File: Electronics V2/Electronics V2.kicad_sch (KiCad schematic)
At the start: 23 parts, among them J1 MOT_L, J2 MOT_R, J3 SD_Card, J4 USB_C_Receptacle_USB2.0_16P, SW1 RST, SW3 RST, SW4 BOOT, U3 ESP32-S3-WROOM-1, U4 DAC081C081CIMK, U5 IMU_L, U6 IMU_R

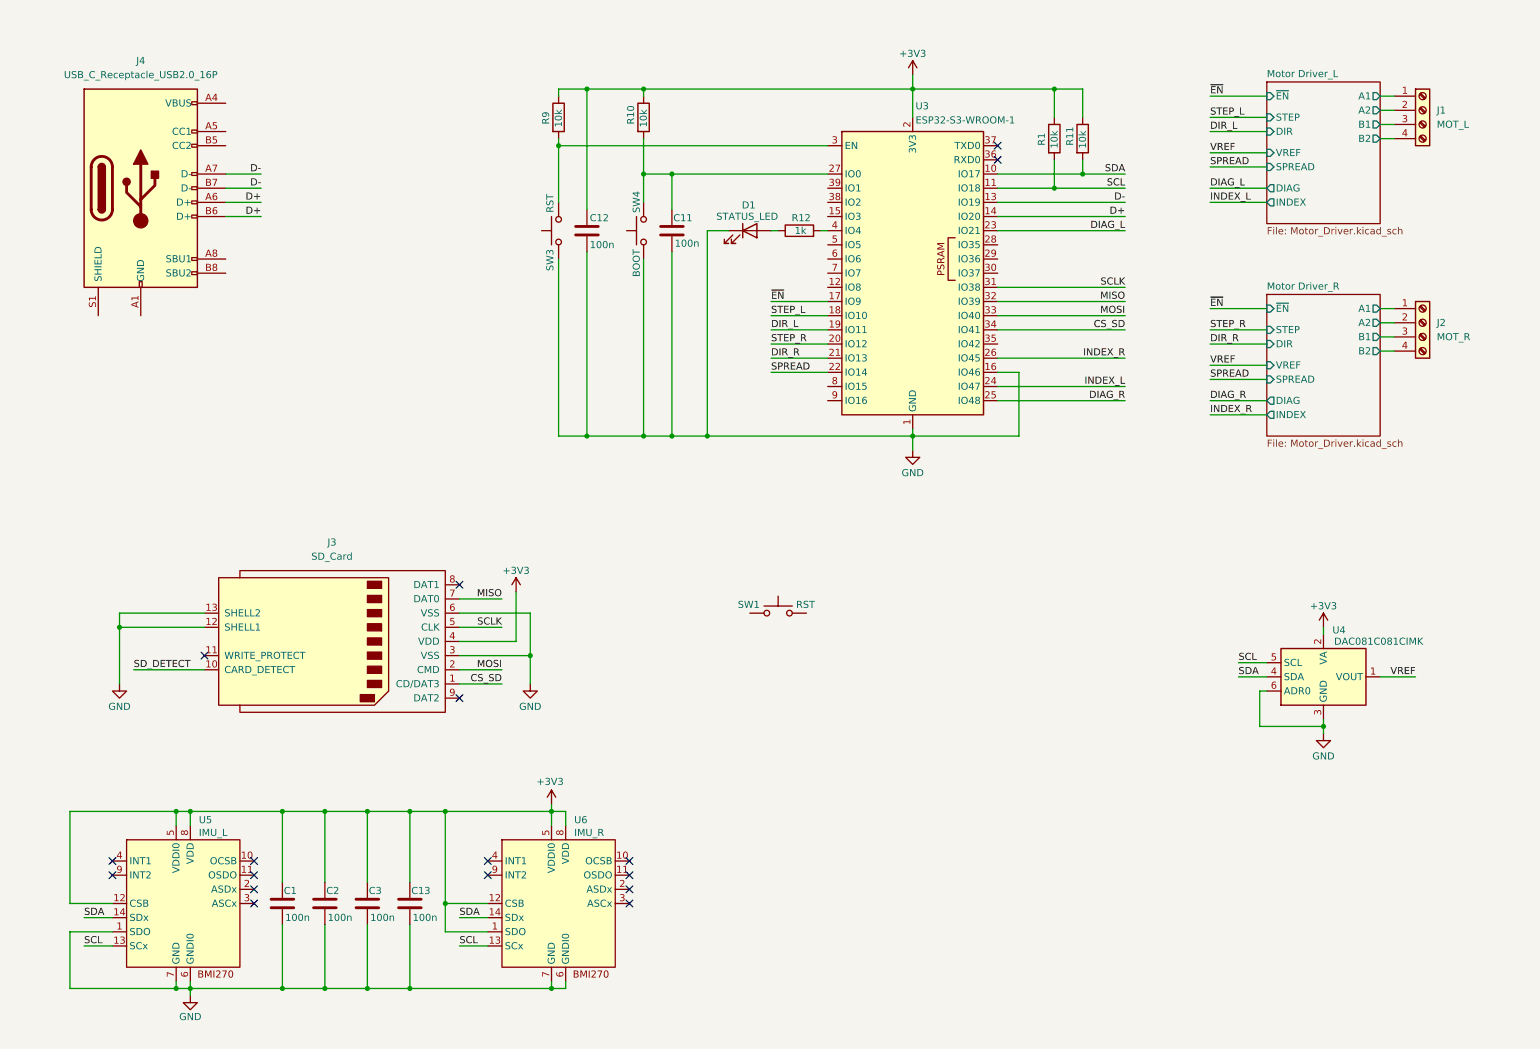
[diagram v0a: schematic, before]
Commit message: rotary encoder, buttons, needs esd, reverse voltage, usb, reg
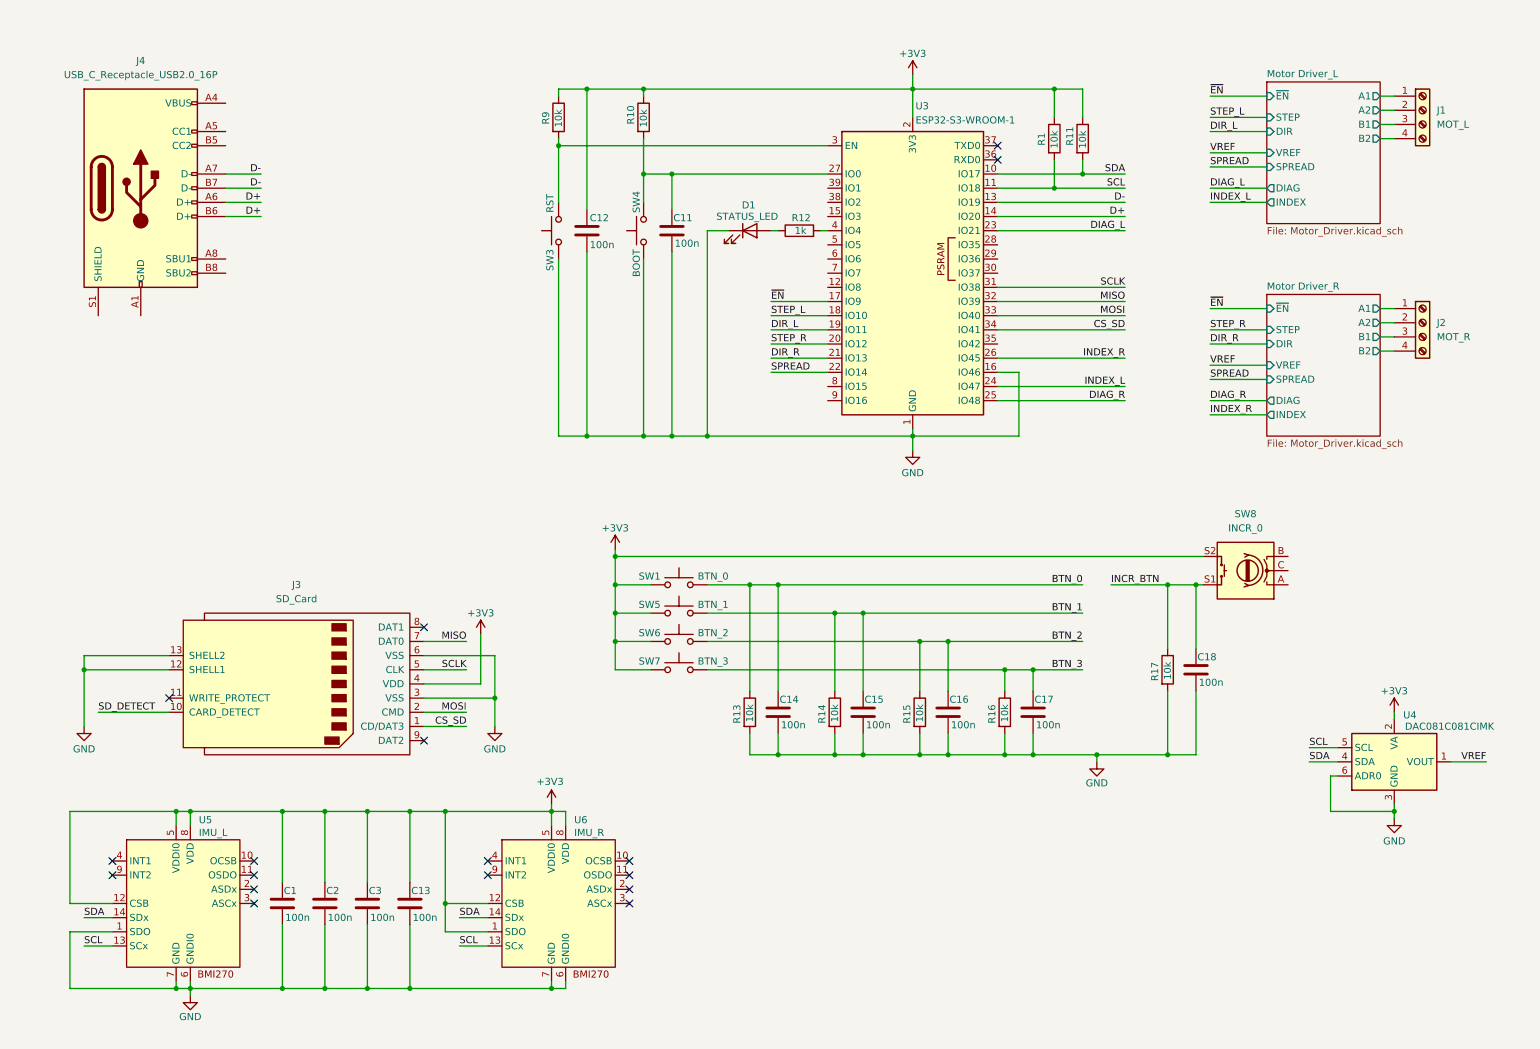
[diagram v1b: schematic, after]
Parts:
- added C14, C15, C16, C17, C18: 100n, symbol Device:C
- added R13, R14, R15, R16, R17: 10k, symbol Device:R
- added SW5: BTN_1, symbol Switch:SW_Push
- added SW6: BTN_2, symbol Switch:SW_Push
- added SW7: BTN_3, symbol Switch:SW_Push
- added SW8: INCR_0, symbol Device:RotaryEncoder_Switch
- SW1: value RST -> BTN_0
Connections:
- net +3V3: now also SW1.1, SW5.1, SW6.1, SW7.1, SW8.S2
- net GND: now also C14.2, C15.2, C16.2, C17.2, C18.2, R13.2, R14.2, R15.2, R16.2, R17.2
- net BTN_0: now reaches SW1.2
- net BTN_0: now also C14.1, R13.1
- new net BTN_1: C15.1, R14.1, SW5.2
- new net BTN_2: C16.1, R15.1, SW6.2
- new net BTN_3: C17.1, R16.1, SW7.2
- new net INCR_BTN: C18.1, R17.1, SW8.S1
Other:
- moved on the sheet: J3, SW1, U4

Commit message: voltage regulators and oled
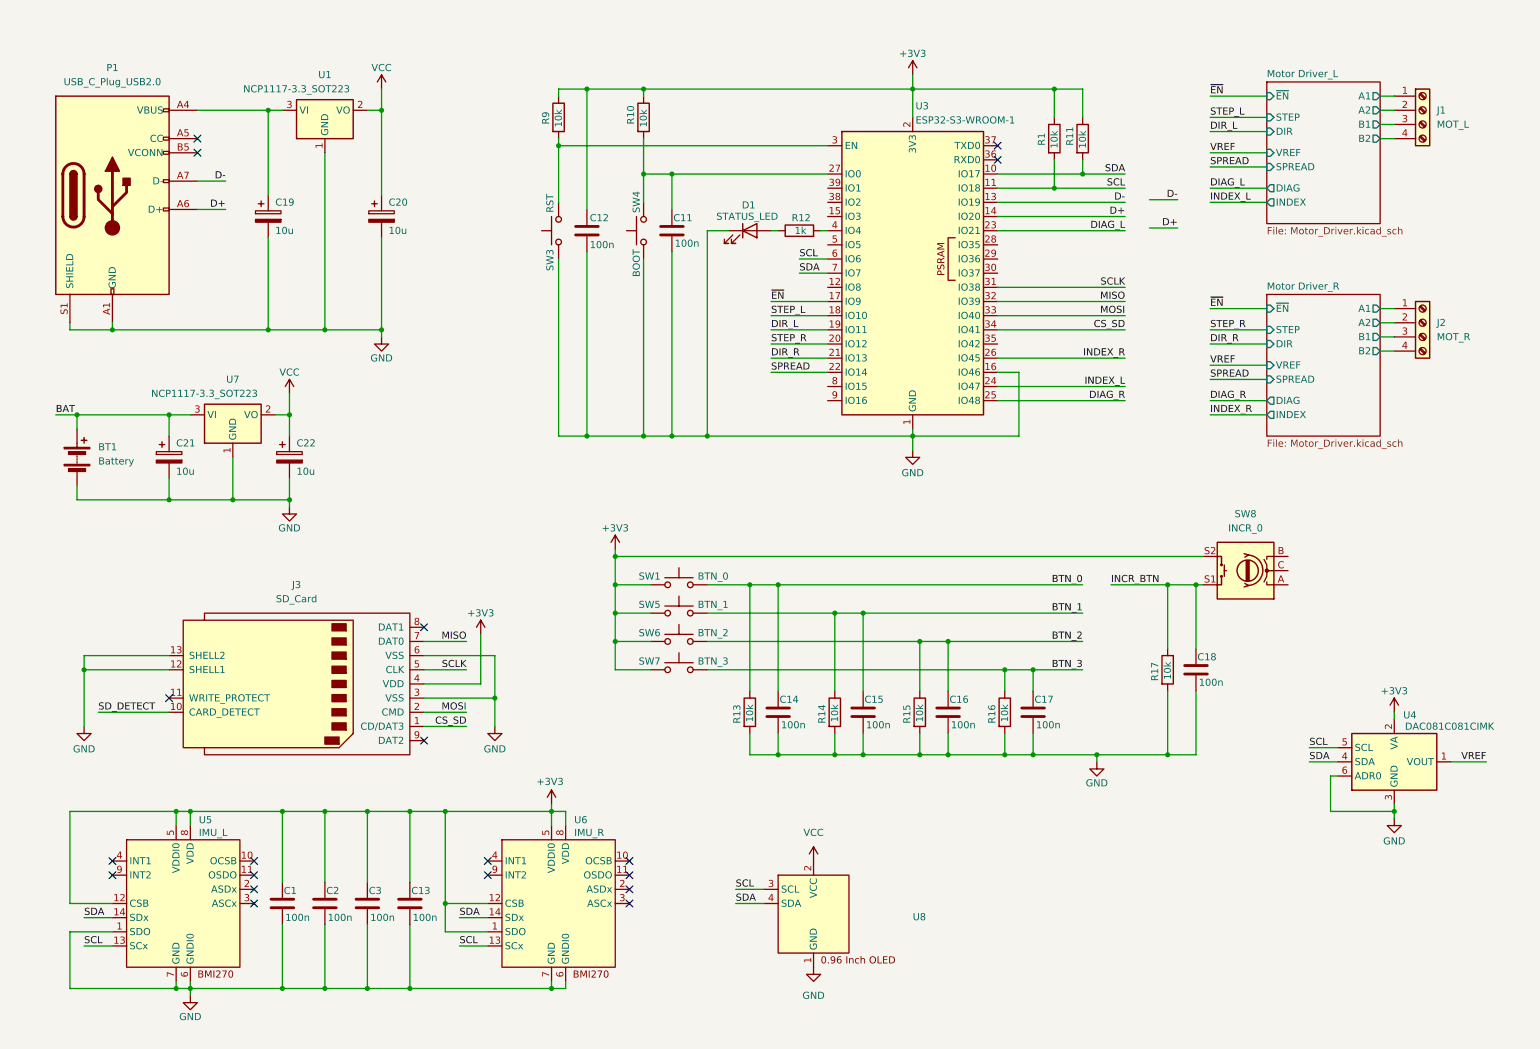
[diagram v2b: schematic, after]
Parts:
- removed J4: USB_C_Receptacle_USB2.0_16P, symbol Connector:USB_C_Receptacle_USB2.0_16P
- added BT1: Battery, TerminalBlock_Phoenix:TerminalBlock_Phoenix_PT-1,5-2-3.5-H_1x02_P3.50mm_Horizontal, symbol Device:Battery
- added C19, C20, C21, C22: 10u, Capacitor_SMD:C_0603_1608Metric, symbol Device:C_Polarized
- added P1: USB_C_Plug_USB2.0, Connector_USB:USB_C_Receptacle_GCT_USB4110, symbol Connector:USB_C_Plug_USB2.0
- added U1, U7: NCP1117-3.3_SOT223, Package_TO_SOT_SMD:SOT-223-3_TabPin2, symbol Regulator_Linear:NCP1117-3.3_SOT223
- added U8: ~, Connector_PinHeader_2.54mm:PinHeader_1x04_P2.54mm_Vertical, symbol 0.96InchOLED:0.96_Inch_OLED
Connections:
- net D+: now also P1.A6 (D+)
- net D-: now also P1.A7 (D-)
- net GND: now also BT1.2 (-), C19.2, C20.2, C21.2, C22.2, P1.A1 (GND), P1.A12 (GND), P1.B1 (GND), P1.B12 (GND), P1.S1 (SHIELD), U1.1 (GND), U7.1 (GND), U8.1 (GND)
- net SCL: now also U3.6 (IO6), U8.3 (SCL)
- net SDA: now also U3.7 (IO7), U8.4 (SDA)
- new net: C19.1, P1.A4 (VBUS), P1.A9 (VBUS), P1.B4 (VBUS), P1.B9 (VBUS), U1.3 (VI)
- new net BAT: BT1.1 (+), C21.1, U7.3 (VI)
- new net VCC: C20.1, C22.1, U1.2 (VO), U7.2 (VO), U8.2 (VCC)
- no-connect marks 17 -> 19

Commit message: usb
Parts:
- removed P1: USB_C_Plug_USB2.0, Connector_USB:USB_C_Receptacle_GCT_USB4110, symbol Connector:USB_C_Plug_USB2.0
- added J4: USB_C_Receptacle_USB2.0_14P, symbol Connector:USB_C_Receptacle_USB2.0_14P
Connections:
- net VCC is gone; now on net +3V3: C20.1, C22.1, U1.2 (VO), U7.2 (VO), U8.2 (VCC)
- net D+: now also J4.A6 (D+), J4.B6 (D+)
- net D-: now also J4.A7 (D-), J4.B7 (D-)
- net DIAG_L: now also U3.35 (IO42); no longer U3.23 (IO21)
- net GND: now also J4.A1 (GND), J4.A12 (GND), J4.B1 (GND), J4.B12 (GND), J4.S1 (SHIELD)
- net SCL: no longer U3.6 (IO6)
- net SDA: no longer U3.7 (IO7)
- net at C19.1, U1.3 (VI): now also J4.A4 (VBUS), J4.A9 (VBUS), J4.B4 (VBUS), J4.B9 (VBUS)

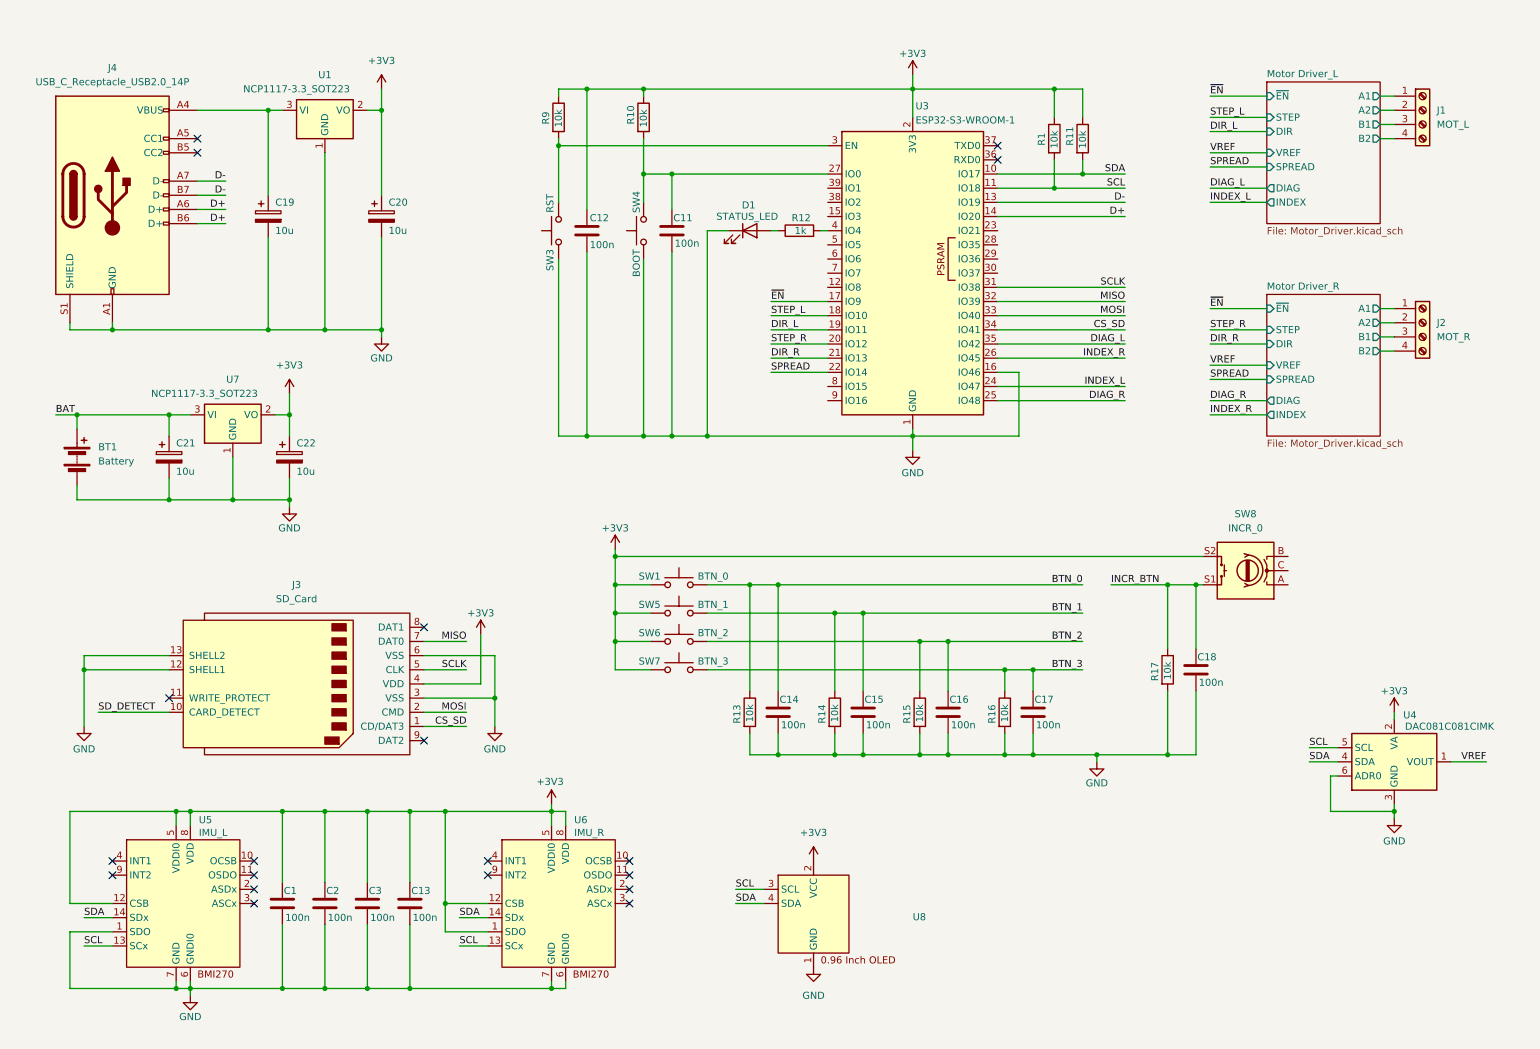
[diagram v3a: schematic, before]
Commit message: needs footprints
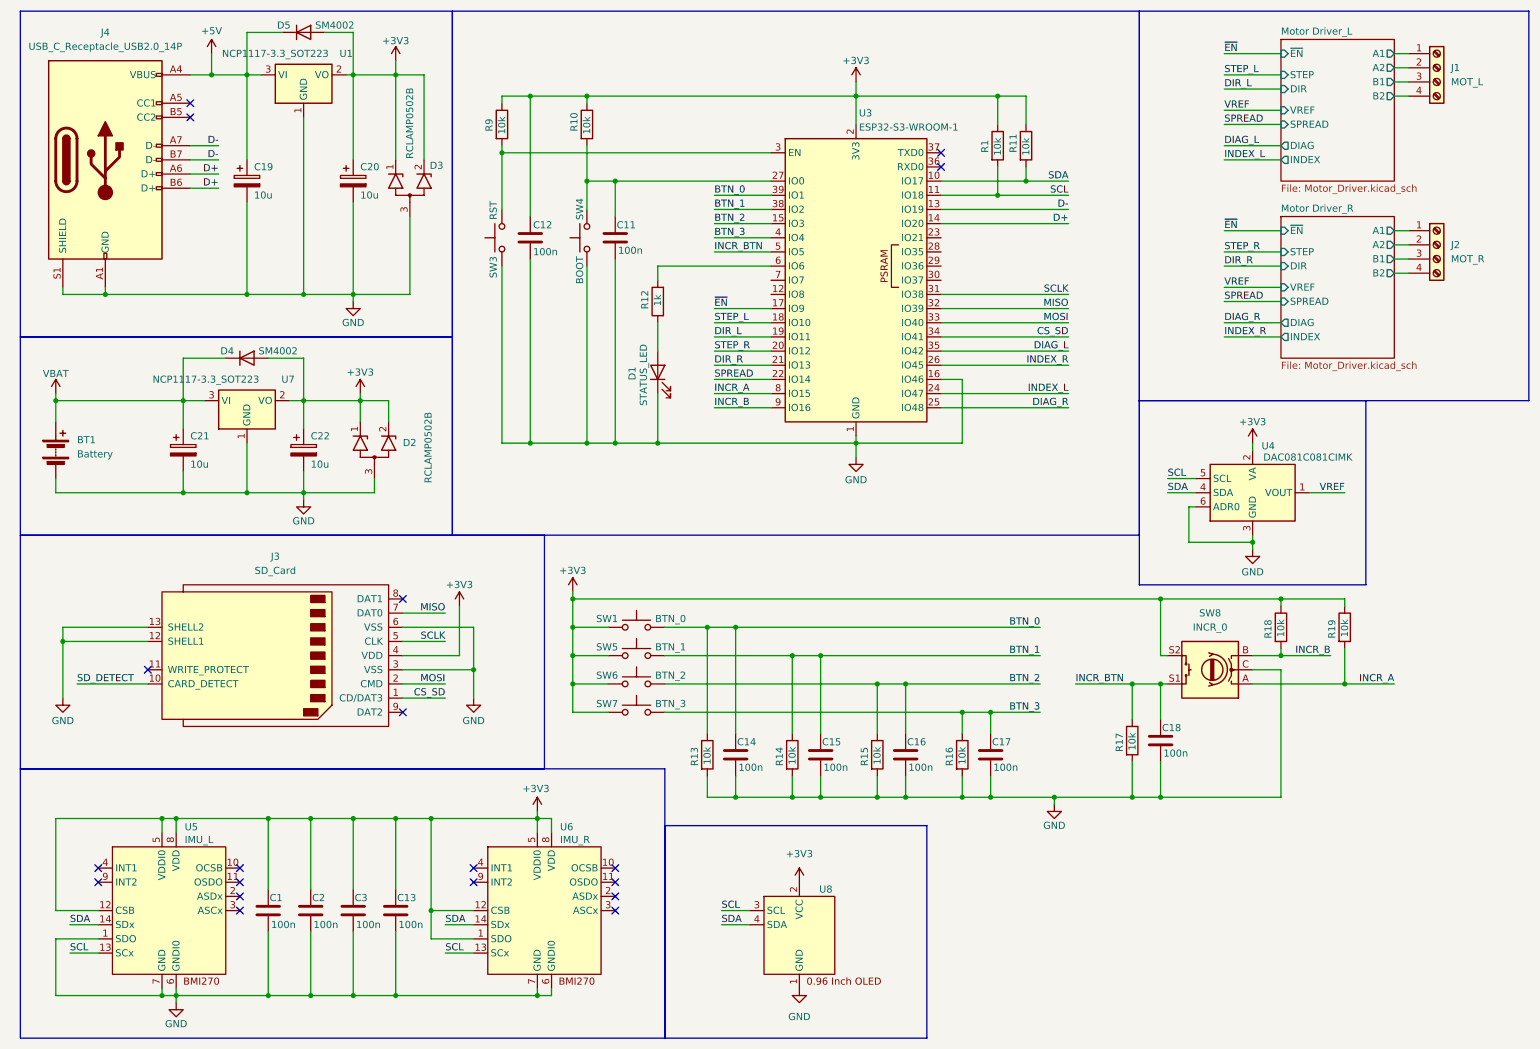
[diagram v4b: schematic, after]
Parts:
- added D2, D3: RCLAMP0502B, Package_TO_SOT_SMD:SOT-416, symbol Power_Protection:RCLAMP0502B
- added D4, D5: SM4002, Diode_SMD:D_MELF, symbol Diode:SM4002
- added R18, R19: 10k, symbol Device:R
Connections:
- net +3V3: now also D2.1 (K1), D2.2 (K2), D3.1 (K1), D3.2 (K2), D4.2 (A), D5.2 (A), R18.1, R19.1
- net BTN_0: now also U3.39 (IO1)
- net BTN_1: now also U3.38 (IO2)
- net BTN_2: now also U3.15 (IO3)
- net BTN_3: now also U3.4 (IO4)
- net GND: now also SW8.C, D2.3 (A), D3.3 (A)
- net INCR_BTN: now also U3.5 (IO5)
- net at R12.2: now also U3.6 (IO6); no longer U3.4 (IO4)
- net +5V: now reaches C19.1, J4.A4 (VBUS), J4.A9 (VBUS), J4.B4 (VBUS), J4.B9 (VBUS), U1.3 (VI)
- net +5V: now also D5.1 (K)
- net INCR_A: now reaches U3.8 (IO15)
- net INCR_A: now also SW8.A, R19.2
- net INCR_B: now reaches U3.9 (IO16)
- net INCR_B: now also SW8.B, R18.2
- net BAT renamed VBAT
- net VBAT: now also D4.1 (K)
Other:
- moved on the sheet: BT1, C1, C11, C12, C13, C14, C15, C16, C17, C18, C19, C2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
